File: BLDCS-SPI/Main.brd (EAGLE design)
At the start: 27.9 x 73.7 mm, 60 parts, among them IC1 MEGA8-AI, IC3 TP4056, J1 PIC_ICSP_MINI_5_PIN, U4 LM1117 3.3, X1 MINI-USB-32005-201, Y1 16MHZ

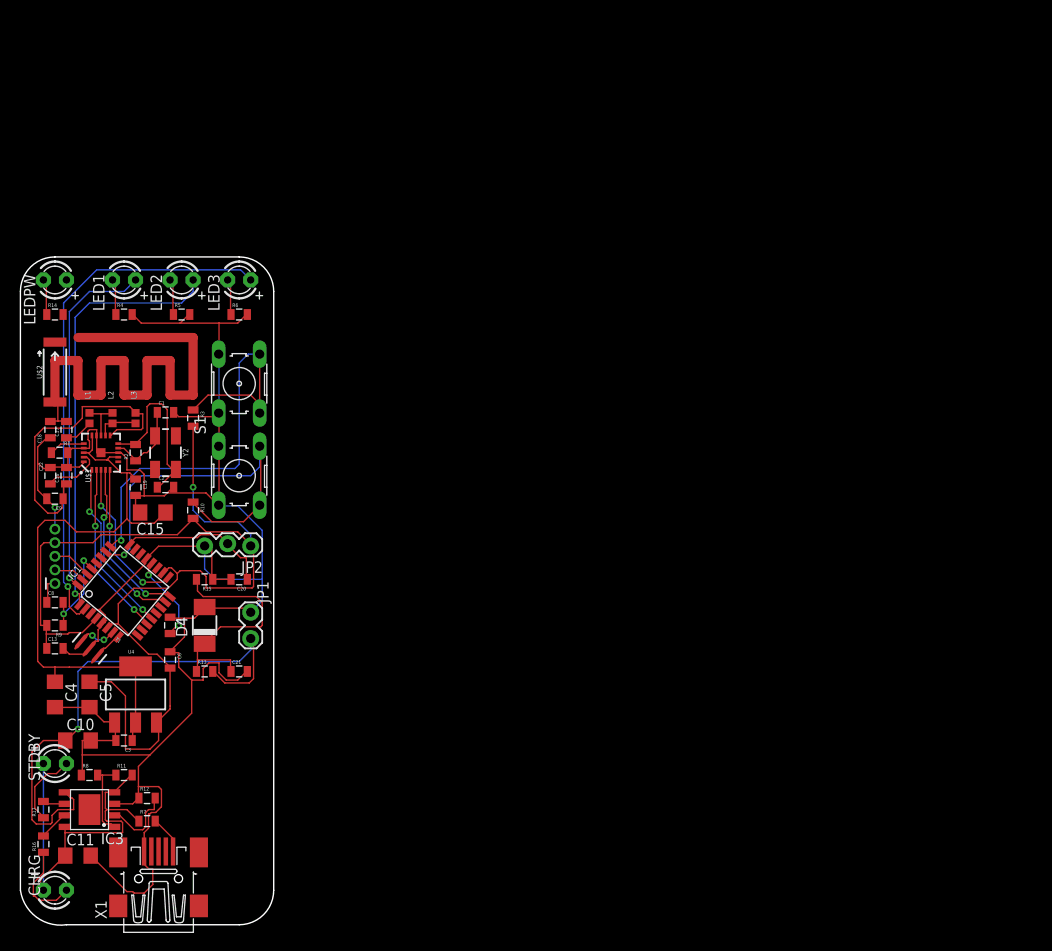
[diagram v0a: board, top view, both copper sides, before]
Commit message: add license
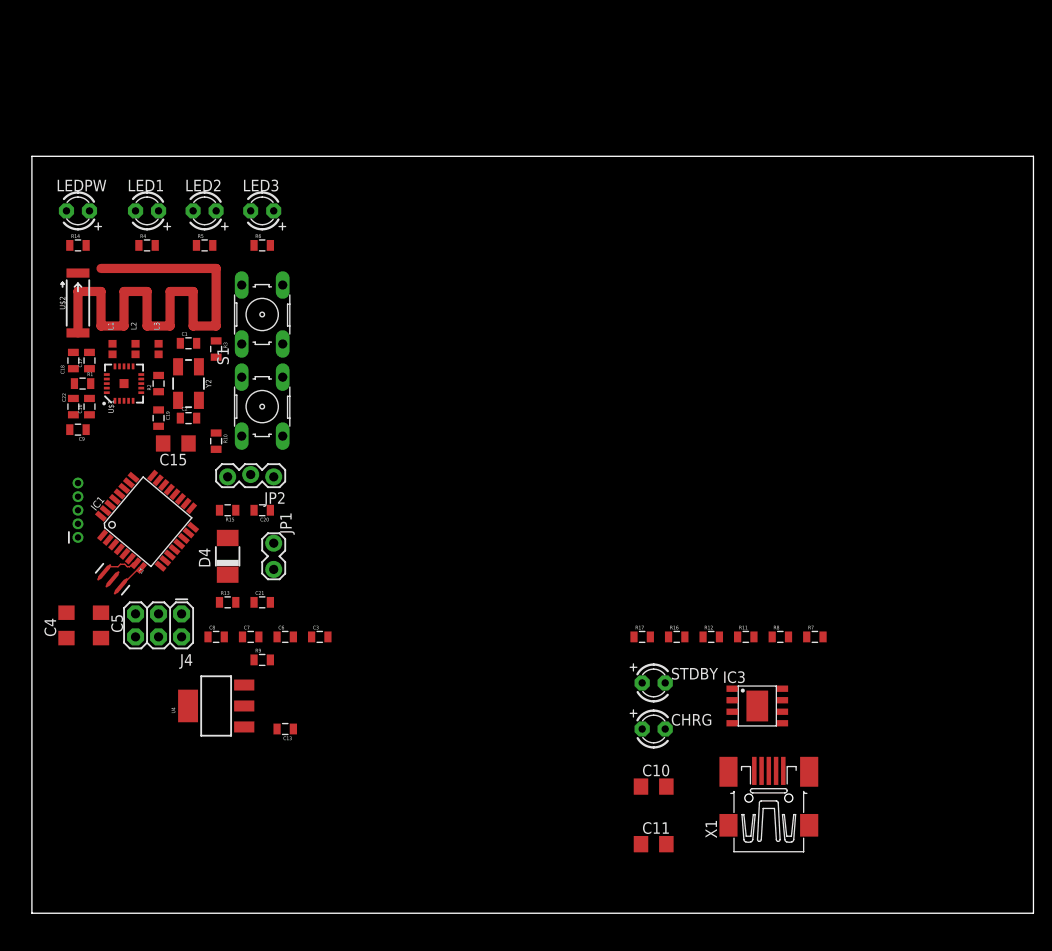
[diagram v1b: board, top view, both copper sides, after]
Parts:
- added J4: SPI, SparkFun-Connectors:2X3
- moved R8 77.7 mm to (82.5, 30.5)
- moved R7 76.4 mm to (86.4, 30.5)
- moved IC3 74.5 mm to (80.0, 22.9), turned to 0 degrees
- moved R16 73.5 mm to (71.1, 30.5), turned to 0 degrees
- moved R11 70.3 mm to (78.7, 30.5)
- moved R17 68.7 mm to (67.3, 30.5), turned to 0 degrees
- moved CHRG 68.4 mm to (68.6, 20.3)
- moved X1 67.9 mm to (81.3, 12.7)
- moved STDBY 66.6 mm to (68.6, 25.4)
- moved R12 64.7 mm to (74.9, 30.5)
- moved C10 63.7 mm to (68.6, 14.0)
- moved C11 63.5 mm to (68.6, 7.62)
- moved C13 26.9 mm to (27.9, 20.3), turned to 180 degrees
- moved C3 24.4 mm to (31.8, 30.5), turned to 0 degrees
- moved R9 23.2 mm to (25.4, 27.9), turned to 0 degrees
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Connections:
- net GND: now also J4.6
- net MISO: now also J4.1
- net MOSI: now also J4.4
- net RST: now also J4.5
- net SCK: now also J4.3
- net VCC: now also J4.2
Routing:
- net GND: track 242.0 -> 0.00 mm, vias 1 -> 0
- net VCC: track 122.1 -> 0.00 mm, vias 1 -> 0
- net 3.3V: track 67.9 -> 0.00 mm
- net BATT_IN: track 59.6 -> 0.00 mm, vias 1 -> 0
- net D4: track 58.7 -> 0.00 mm, vias 1 -> 0
- net A2: track 51.3 -> 0.00 mm, vias 1 -> 0
- net D3: track 47.6 -> 0.00 mm, vias 1 -> 0
- net A3: track 43.1 -> 0.00 mm, vias 1 -> 0
- net N$25: track 43.0 -> 0.00 mm
- net D2: track 39.4 -> 0.00 mm, vias 1 -> 0
- net N$16: track 33.9 -> 0.00 mm
- net A0: track 27.8 -> 0.00 mm
- net D7: track 19.5 -> 0.00 mm, vias 2 -> 0
- net D8: track 19.5 -> 0.00 mm, vias 2 -> 0
- net N$21: track 19.4 -> 0.00 mm
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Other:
- board size 27.9 x 73.7 mm -> 110.5 x 83.5 mm

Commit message: add license
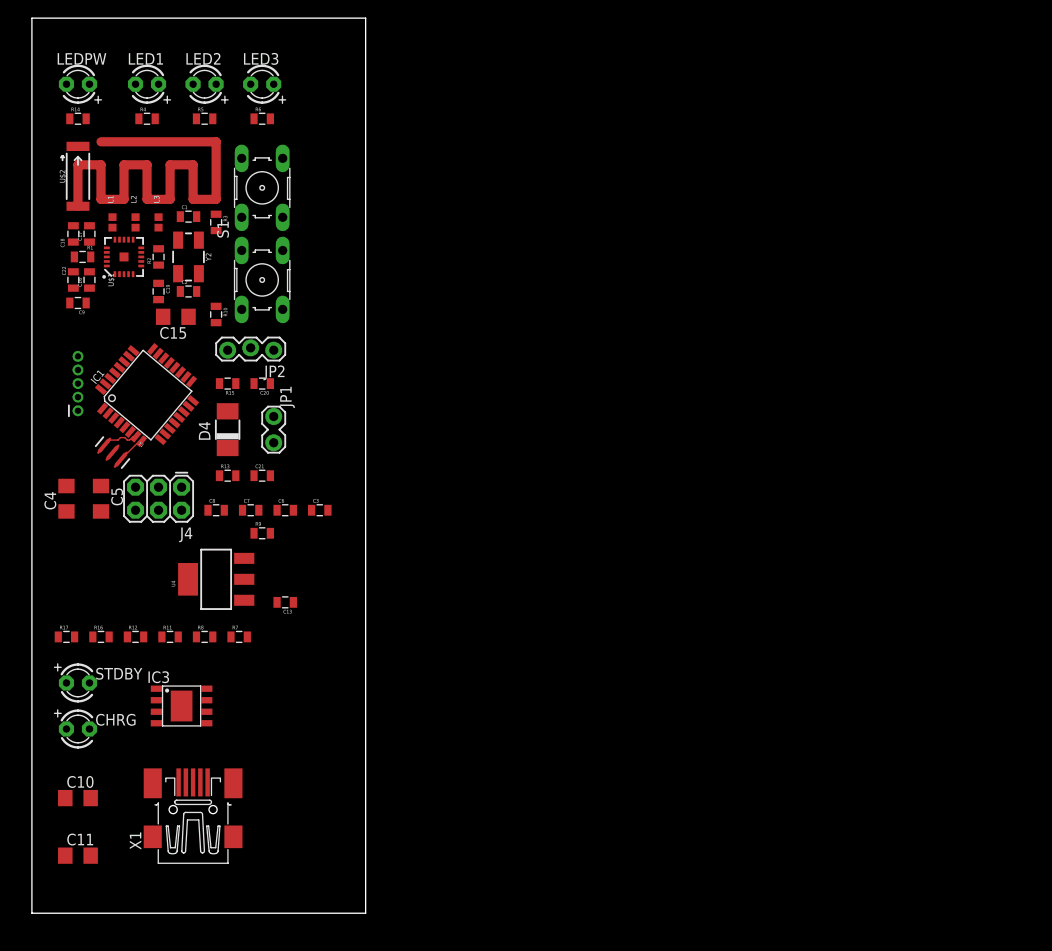
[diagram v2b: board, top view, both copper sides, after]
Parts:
- moved C10 63.5 mm to (5.08, 12.7)
- moved C11 63.5 mm to (5.08, 6.35)
- moved X1 63.5 mm to (17.8, 11.4)
- moved R12 63.5 mm to (11.4, 30.5)
- moved R16 63.5 mm to (7.62, 30.5)
- moved CHRG 63.5 mm to (5.08, 20.3)
- moved IC3 63.5 mm to (16.5, 22.9)
- moved R17 63.5 mm to (3.81, 30.5)
- moved R7 63.5 mm to (22.9, 30.5)
- moved R8 63.5 mm to (19.1, 30.5)
- moved STDBY 63.5 mm to (5.08, 25.4)
- moved R11 63.5 mm to (15.2, 30.5)
- moved C17 14.0 mm to (6.35, 74.9)
- moved C18 14.0 mm to (4.57, 74.9)
- moved D4 14.0 mm to (21.6, 53.3)
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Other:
- board size 110.5 x 83.5 mm -> 36.8 x 98.7 mm
